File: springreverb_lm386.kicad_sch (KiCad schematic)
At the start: 64 parts, among them J1 IN, J10 VR2_3, J11 VR_2_2, J12 To, J13 FromSW, J14 To_Tank, J15 From_Tank, J16 FromGND, J17 From, J18 VR_4_1, J19 VR4_3, J2 INGND, J20 VR3_1, J21 OUT, J3 GND, J4 Vin, J5 LEDGND, J6 VR1_3, J7 VR_1_1, J8 toC6, J9 toC7, SW1 SW_SPDT, SW2 SW_SPST, U1 TL072, U2 TC1044S, U3 LM386

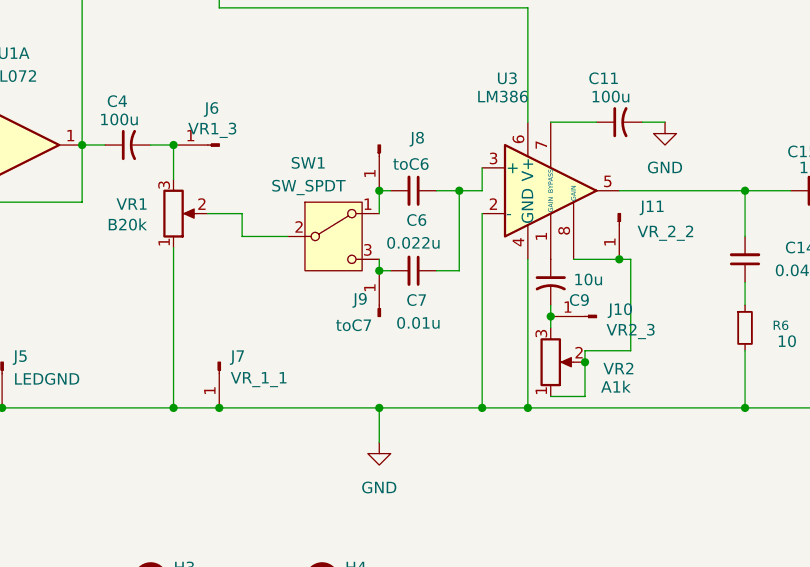
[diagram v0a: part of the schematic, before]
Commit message: 入力のコンデンサの値を変更
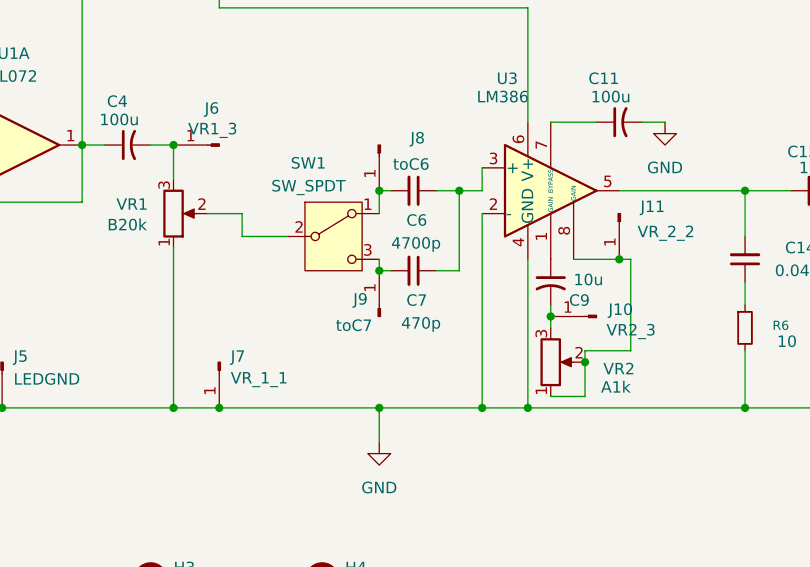
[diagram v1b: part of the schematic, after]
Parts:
- C6: value 0.022u -> 4700p
- C7: value 0.01u -> 470p
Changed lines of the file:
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@@
 			)
 		)
-		(property "Value" "0.022u"
+		(property "Value" "4700p"
 			(at 100.838 144.272 90)
 			(show_name no)
@@
 			)
 		)
-		(property "Value" "0.01u"
+		(property "Value" "470p"
 			(at 100.838 153.162 90)
 			(show_name no)

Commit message: 実際に配線しての修正を反映
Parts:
- removed J19: VR4_3, MyLibrary:PinHeader_1x01_P2.54mm_Vertical, symbol Connector:Conn_01x01_Pin
- removed J2: INGND, MyLibrary:PinHeader_1x01_P2.54mm_Vertical, symbol Connector:Conn_01x01_Pin
- removed J3: GND, MyLibrary:PinHeader_1x01_P2.54mm_Vertical, symbol Connector:Conn_01x01_Pin
- removed J5: LEDGND, MyLibrary:PinHeader_1x01_P2.54mm_Vertical, symbol Connector:Conn_01x01_Pin
- added R4: 10k, symbol Device:R_Small
- added R5: 4k, symbol Device:R_Small
- J15: renamed from J20; value VR3_1 -> VR4_1
- J16: renamed from J18; value VR_4_1 -> VR_3_1
- renumbered C2 to C1, C11 to C10, C12 to C11, C13 to C12, C14 to C13, C15 to C14, C16 to C15, C17 to C16, C18 to C17, C19 to C18, C20 to C19, C3 to C2, C21 to C20, C4 to C3, C5 to C4, C6 to C5, C7 to C6, C8 to C7, C9 to C8, C10 to C9, J13 to J10, J14 to J11, J15 to J12, J16 to J13, J17 to J14, J21 to J17, J4 to J2, J6 to J3, J7 to J4, J8 to J5, J9 to J6, J10 to J7, J11 to J8, J12 to J9, R8 to R10, R9 to R11, R10 to R12, R4 to R6, R5 to R7, R6 to R8, R7 to R9
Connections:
- net GND: now also R5.1
- net at SW1.2 (B): now also R4.2, R5.2; no longer VR1.2
- new net: R4.1, VR1.2

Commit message: GNDの位置を修正
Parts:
- removed J4: VR_1_1, MyLibrary:PinHeader_1x01_P2.54mm_Vertical, symbol Connector:Conn_01x01_Pin
- added J3: GND, MyLibrary:PinHeader_1x01_P2.54mm_Vertical, symbol Connector:Conn_01x01_Pin
- renumbered J9 to J10, J10 to J11, J11 to J12, J12 to J13, J13 to J14, J14 to J15, J15 to J16, J16 to J17, J17 to J18, J3 to J4, J5 to J6, J6 to J7, J7 to J8, J8 to J9
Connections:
- net GND: now also J3.1 (Pin_1)
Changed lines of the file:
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@@
 	)
 	(junction
-		(at 76.2 162.56)
+		(at 58.42 91.44)
 		(diameter 0)
 		(color 0 0 0 0)
@@
 	(wire
 		(pts
-			(xy 76.2 162.56) (xy 105.41 162.56)
+			(xy 71.12 162.56) (xy 105.41 162.56)
 		)
 		(stroke
@@
 	(wire
 		(pts
-			(xy 71.12 162.56) (xy 76.2 162.56)
-		)
-		(stroke
-			(width 0)
-			(type default)
-		)
-	)
-	(wire
-		(pts
 			(xy 100.33 147.32) (xy 102.87 147.32)
 		)
@@
 		(dnp no)
 		(fields_autoplaced yes)
-		(property "Reference" "J10"
+		(property "Reference" "J11"
 			(at 160.655 153.67 0)
 			(show_name no)
@@
 			(project "springreverb_lm386"
 				(path "/db334565-2b42-4a43-9204-0bb0e555e376"
-					(reference "J10")
+					(reference "J11")
 					(unit 1)
 				)
@@
 		(dnp no)
 		(fields_autoplaced yes)
-		(property "Reference" "J13"
+		(property "Reference" "J14"
 			(at 178.435 142.24 0)
 			(show_name no)
@@
 			(project "springreverb_lm386"
 				(path "/db334565-2b42-4a43-9204-0bb0e555e376"
-					(reference "J13")
-					(unit 1)
-				)
-			)
-		)
-	)
-	(symbol
-		(lib_id "Connector:Conn_01x01_Pin")
-		(at 76.2 157.48 270)
-		(unit 1)
-		(body_style 1)
-		(exclude_from_sim no)
-		(in_bom yes)
-		(on_board yes)
-		(in_pos_files yes)
-		(dnp no)
-		(property "Reference" "J4"
-			(at 77.47 156.8449 90)
-			(show_name no)
-			(do_not_autoplace no)
-			(effects
-				(font
-					(size 1.27 1.27)
-				)
-				(justify left)
-			)
-		)
-		(property "Value" "VR_1_1"
-			(at 77.47 159.258 90)
-			(show_name no)
-			(do_not_autoplace no)
-			(effects
-				(font
-					(size 1.27 1.27)
-				)
-				(justify left)
-			)
-		)
-		(property "Footprint" "MyLibrary:PinHeader_1x01_P2.54mm_Vertical"
-			(at 76.2 157.48 0)
-			(hide yes)
-			(show_name no)
-			(do_not_autoplace no)
-			(effects
-				(font
-					(size 1.27 1.27)
-				)
-			)
-		)
-		(property "Datasheet" ""
-			(at 76.2 157.48 0)
-			(hide yes)
-			(show_name no)
-			(do_not_autoplace no)
-			(effects
-				(font
-					(size 1.27 1.27)
-				)
-			)
-		)
-		(property "Description" "Generic connector, single row, 01x01, script generated"
-			(at 76.2 157.48 0)
-			(hide yes)
-			(show_name no)
-			(do_not_autoplace no)
-			(effects
-				(font
-					(size 1.27 1.27)
-				)
-			)
-		)
-		(pin "1"
-		)
-		(instances
-			(project "springreverb_lm386"
-				(path "/db334565-2b42-4a43-9204-0bb0e555e376"
-					(reference "J4")
+					(reference "J14")
 					(unit 1)
 				)
@@
 		(in_pos_files yes)
 		(dnp no)
-		(property "Reference" "J16"
+		(property "Reference" "J17"
 			(at 217.678 141.478 0)
 			(show_name no)
@@
 			(project "springreverb_lm386"
 				(path "/db334565-2b42-4a43-9204-0bb0e555e376"
-					(reference "J16")
+					(reference "J17")
 					(unit 1)
 				)
@@
 		(in_pos_files yes)
 		(dnp no)
-		(property "Reference" "J5"
+		(property "Reference" "J6"
 			(at 99.06 132.588 90)
 			(show_name no)
@@
 			(project "springreverb_lm386"
 				(path "/db334565-2b42-4a43-9204-0bb0e555e376"
-					(reference "J5")
+					(reference "J6")
 					(unit 1)
 				)
@@
 		(in_pos_files yes)
 		(dnp no)
-		(property "Reference" "J15"
+		(property "Reference" "J16"
 			(at 218.44 120.396 0)
 			(show_name no)
@@
 			(project "springreverb_lm386"
 				(path "/db334565-2b42-4a43-9204-0bb0e555e376"
-					(reference "J15")
+					(reference "J16")
 					(unit 1)
 				)
@@
 		(dnp no)
 		(fields_autoplaced yes)
-		(property "Reference" "J14"
+		(property "Reference" "J15"
 			(at 181.61 132.7149 90)
 			(show_name no)
@@
 			(project "springreverb_lm386"
 				(path "/db334565-2b42-4a43-9204-0bb0e555e376"
-					(reference "J14")
+					(reference "J15")
 					(unit 1)
 				)
@@
 		(in_pos_files yes)
 		(dnp no)
-		(property "Reference" "J8"
+		(property "Reference" "J9"
 			(at 125.73 140.208 90)
 			(show_name no)
@@
 			(project "springreverb_lm386"
 				(path "/db334565-2b42-4a43-9204-0bb0e555e376"
-					(reference "J8")
+					(reference "J9")
 					(unit 1)
 				)
@@
 		(in_pos_files yes)
 		(dnp no)
-		(property "Reference" "J11"
+		(property "Reference" "J12"
 			(at 162.306 133.096 0)
 			(show_name no)
@@
 			(project "springreverb_lm386"
 				(path "/db334565-2b42-4a43-9204-0bb0e555e376"
-					(reference "J11")
+					(reference "J12")
 					(unit 1)
 				)
@@
 		(in_pos_files yes)
 		(dnp no)
-		(property "Reference" "J7"
+		(property "Reference" "J8"
 			(at 122.174 151.638 0)
 			(show_name no)
@@
 			(project "springreverb_lm386"
 				(path "/db334565-2b42-4a43-9204-0bb0e555e376"
-					(reference "J7")
+					(reference "J8")
 					(unit 1)
 				)
@@
 		(in_pos_files yes)
 		(dnp no)
-		(property "Reference" "J17"
+		(property "Reference" "J18"
 			(at 244.475 125.73 0)
 			(show_name no)
@@
 			(project "springreverb_lm386"
 				(path "/db334565-2b42-4a43-9204-0bb0e555e376"
-					(reference "J17")
+					(reference "J18")
 					(unit 1)
 				)
@@
 		(in_pos_files yes)
 		(dnp no)
-		(property "Reference" "J3"
+		(property "Reference" "J4"
 			(at 76.2 129.286 0)
 			(show_name no)
@@
 			(project "springreverb_lm386"
 				(path "/db334565-2b42-4a43-9204-0bb0e555e376"
-					(reference "J3")
+					(reference "J4")
 					(unit 1)
 				)
@@
 		(in_pos_files yes)
 		(dnp no)
-		(property "Reference" "J12"
+		(property "Reference" "J13"
 			(at 175.006 131.318 0)
 			(show_name no)
@@
 			(project "springreverb_lm386"
 				(path "/db334565-2b42-4a43-9204-0bb0e555e376"
-					(reference "J12")
+					(reference "J13")
 					(unit 1)
 				)
@@
 		(in_pos_files yes)
 		(dnp no)
-		(property "Reference" "J9"
+		(property "Reference" "J10"
 			(at 152.4 131.064 90)
 			(show_name no)
@@
 			(project "springreverb_lm386"
 				(path "/db334565-2b42-4a43-9204-0bb0e555e376"
-					(reference "J9")
+					(reference "J10")
 					(unit 1)
 				)
@@
 	)
 	(symbol
+		(lib_id "Connector:Conn_01x01_Pin")
+		(at 53.34 91.44 0)
+		(unit 1)
+		(body_style 1)
+		(exclude_from_sim no)
+		(in_bom yes)
+		(on_board yes)
+		(in_pos_files yes)
+		(dnp no)
+		(property "Reference" "J3"
+			(at 50.4825 85.4074 0)
+			(show_name no)
+			(do_not_autoplace no)
+			(effects
+				(font
+					(size 1.27 1.27)
+				)
+				(justify left)
+			)
+		)
+		(property "Value" "GND"
+			(at 50.4825 87.8205 0)
+			(show_name no)
+			(do_not_autoplace no)
+			(effects
+				(font
+					(size 1.27 1.27)
+				)
+				(justify left)
+			)
+		)
+		(property "Footprint" "MyLibrary:PinHeader_1x01_P2.54mm_Vertical"
+			(at 53.34 91.44 0)
+			(hide yes)
+			(show_name no)
+			(do_not_autoplace no)
+			(effects
+				(font
+					(size 1.27 1.27)
+				)
+			)
+		)
+		(property "Datasheet" ""
+			(at 53.34 91.44 0)
+			(hide yes)
+			(show_name no)
+			(do_not_autoplace no)
+			(effects
+				(font
+					(size 1.27 1.27)
+				)
+			)
+		)
+		(property "Description" "Generic connector, single row, 01x01, script generated"
+			(at 53.34 91.44 0)
+			(hide yes)
+			(show_name no)
+			(do_not_autoplace no)
+			(effects
+				(font
+					(size 1.27 1.27)
+				)
+			)
+		)
+		(pin "1"
+		)
+		(instances
+			(project "springreverb_lm386"
+				(path "/db334565-2b42-4a43-9204-0bb0e555e376"
+					(reference "J3")
+					(unit 1)
+				)
+			)
+		)
+	)
+	(symbol
 		(lib_id "Device:R_Potentiometer")
 		(at 71.12 140.97 0)
@@
 		(in_pos_files yes)
 		(dnp no)
-		(property "Reference" "J6"
+		(property "Reference" "J7"
 			(at 92.71 150.4949 90)
 			(show_name no)
@@
 			(project "springreverb_lm386"
 				(path "/db334565-2b42-4a43-9204-0bb0e555e376"
-					(reference "J6")
+					(reference "J7")
 					(unit 1)
 				)

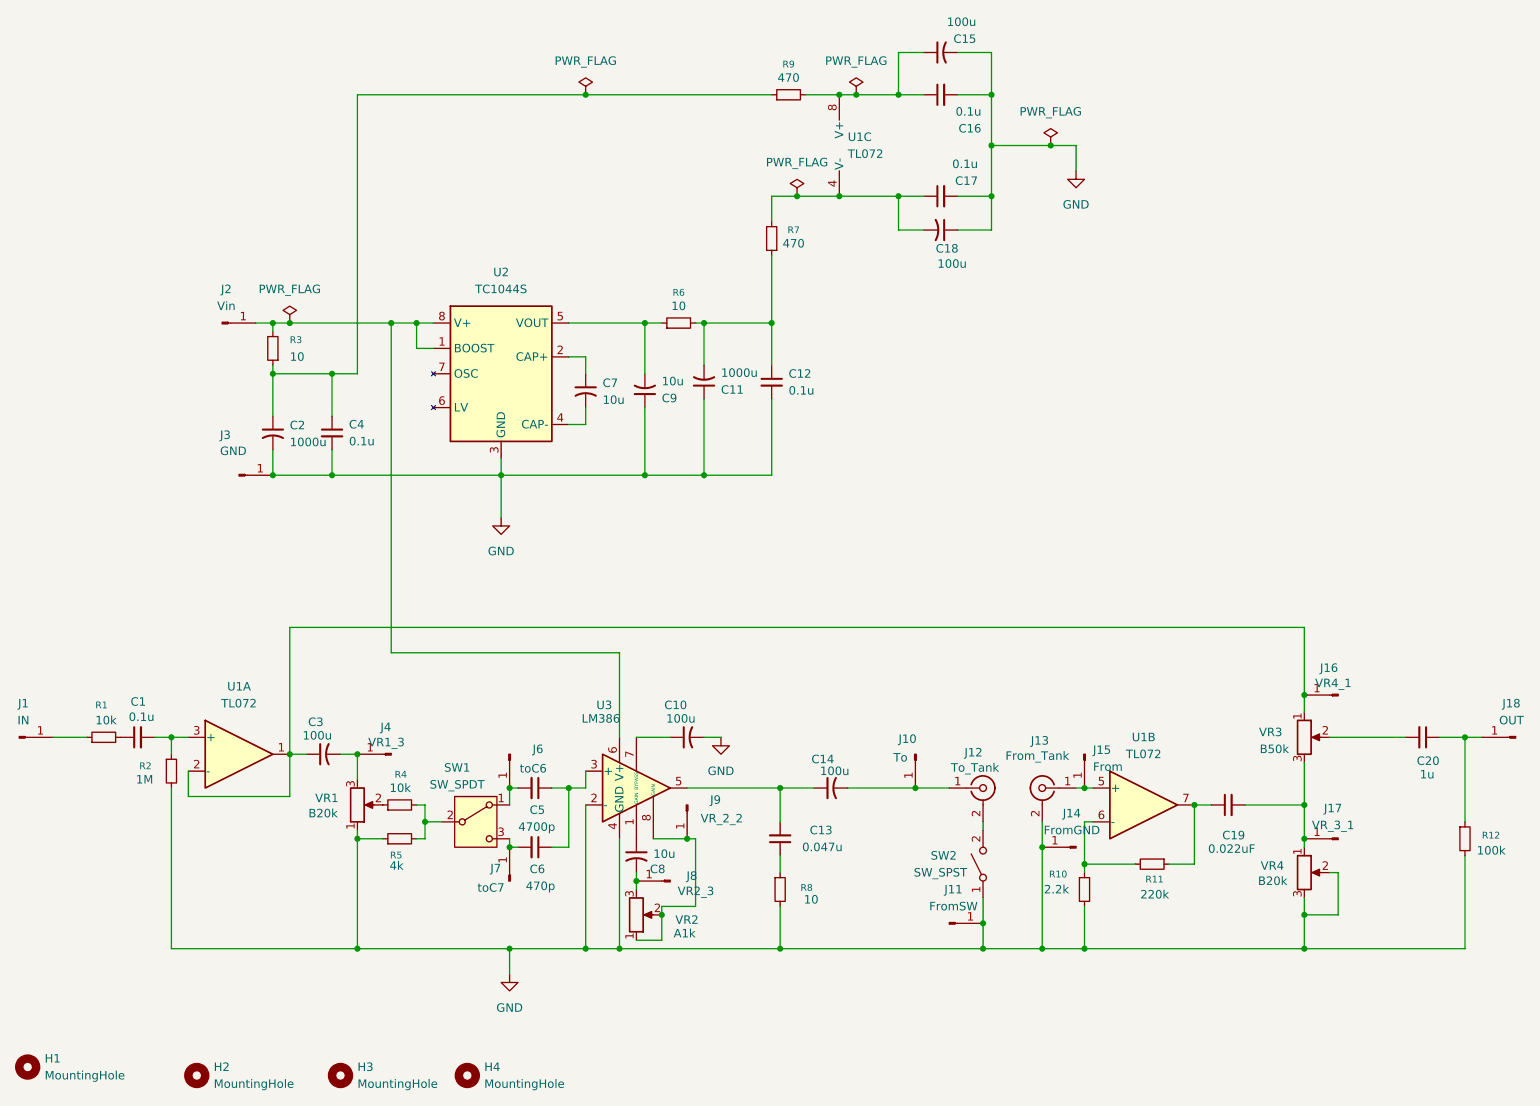
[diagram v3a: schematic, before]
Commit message: トーン回路の修正
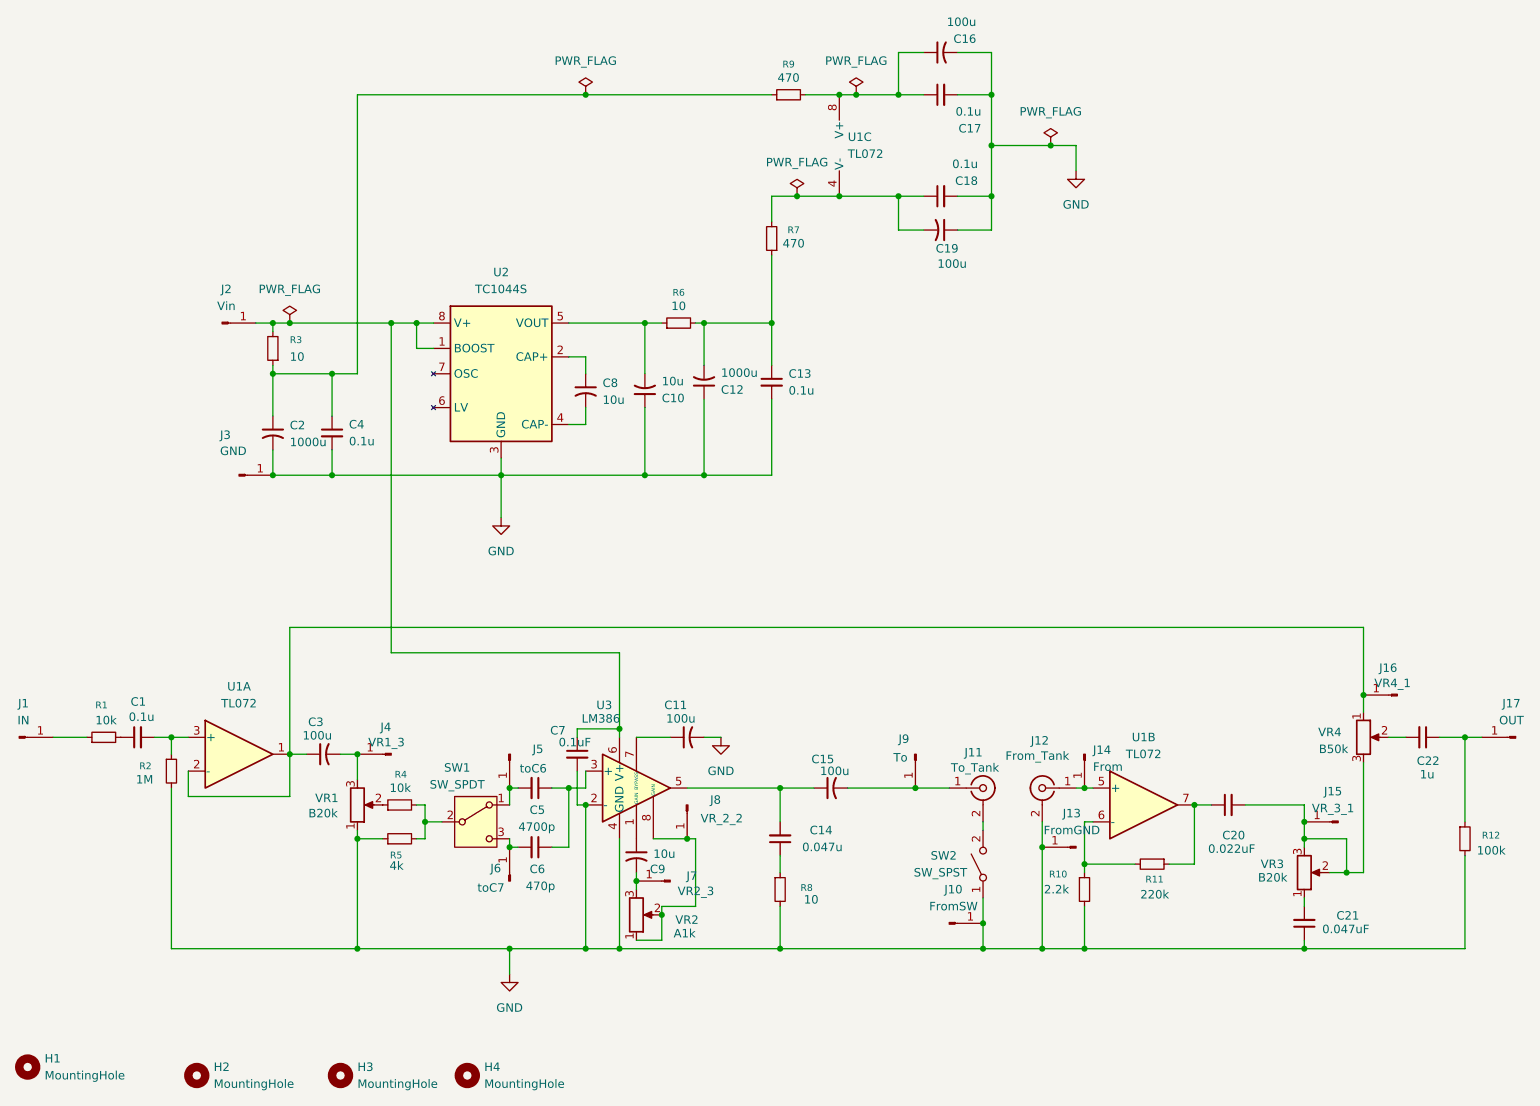
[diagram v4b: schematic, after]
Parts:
- added C21: 0.047uF, symbol Device:C_Small
- added C7: 0.1uF, symbol Device:C_Small
- renumbered C9 to C10, C10 to C11, C11 to C12, C12 to C13, C13 to C14, C14 to C15, C15 to C16, C16 to C17, C17 to C18, C18 to C19, C19 to C20, C20 to C22, C7 to C8, C8 to C9, J11 to J10, J12 to J11, J13 to J12, J14 to J13, J15 to J14, J17 to J15, J18 to J17, J6 to J5, J7 to J6, J8 to J7, J9 to J8, J10 to J9, VR4 to VR3, VR3 to VR4
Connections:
- net GND: now also C21.1, C7.2; no longer VR3.2, VR3.3
- net at C20.2, J15.1 (Pin_1), VR4.3: now also VR3.2, VR3.3; no longer VR3.1
- net at J2.1 (Pin_1), R3.2, U2.1 (BOOST)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: now also C7.1
- new net: C21.2, VR3.1
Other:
- moved on the sheet: J15, J16, VR4
